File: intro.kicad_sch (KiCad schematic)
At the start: 122 parts, among them IC1 IS31FL3741A-QFLS4-TR, SW1 SW_Push, SW10 SW_Push, SW11 SW_Push, SW12 SW_Push, SW13 SW_Push, SW14 SW_Push, SW15 SW_Push, SW16 SW_Push, SW17 SW_Push, SW18 SW_Push, SW19 SW_Push, SW2 SW_Push, SW20 SW_Push, SW21 SW_Push, SW22 SW_Push, SW23 SW_Push, SW24 SW_Push, SW25 SW_Push, SW26 SW_Push, SW27 SW_Push, SW28 SW_Push, SW29 SW_Push, SW3 SW_Push, SW30 SW_Push, SW31 SW_Push, SW32 SW_Push, SW33 SW_Push, SW34 SW_Push, SW35 RotaryEncoder_Switch, SW4 SW_Push, SW5 SW_Push, SW6 SW_Push, SW7 SW_Push, SW8 SW_Push, SW9 SW_Push, U1 nice_nano

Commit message: Set up LED routing
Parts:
- removed S1, S2: Choc_stab, intro:Kailh-PG1350-2u-STAB, symbol marbastlib-mx:MX_stab
- added C10, C2, C8: 0.1μF, Capacitor_SMD:C_0805_2012Metric, symbol Device:C_Small
- added C3, C9: 1μF, Capacitor_SMD:C_0805_2012Metric, symbol Device:C_Small
- added IC2: IS31FL3741A-QFLS4-TR, QFN40P700X700X80-61N-D, symbol IS31FL3741A-QFLS4-TR:IS31FL3741A-QFLS4-TR
- added R10: 10kΩ, Resistor_SMD:R_0805_2012Metric, symbol Device:R_Small_US
- added R6, R9: 100kΩ, Resistor_SMD:R_0805_2012Metric, symbol Device:R_Small_US
- added R7, R8: 2kΩ, Resistor_SMD:R_0805_2012Metric, symbol Device:R_Small_US
- D1, D10, D11, D12, D13, D14, D15, D16, D17, D18, D19, D2, D20, D21, D22, D23, D24, D25, D26, D27, D28, D29, D3, D30, D31, D32, D33, D34, D35, D4, D5, D6, D7, D8, D9: footprint Diode_SMD:D_SOD-123 -> intro:D_SOD-123_Reversible
- LED1, LED10, LED11, LED12, LED13, LED14, LED15, LED16, LED17, LED18, LED19, LED2, LED20, LED21, LED22, LED23, LED24, LED25, LED26, LED27, LED28, LED29, LED3, LED30, LED31, LED32, LED33, LED34, LED35, LED36, LED37, LED4, LED5, LED6, LED7, LED8, LED9: footprint intro:FMB2020RGBAHG -> intro:FMB2020RGBAHG_Reversible
- SW1, SW14, SW15, SW29, SW33: footprint intro:SW_choc_1.5u -> intro:SW_choc_Reversible_1.5u
- SW10, SW11, SW12, SW13, SW16, SW17, SW18, SW19, SW2, SW20, SW21, SW22, SW23, SW24, SW25, SW26, SW27, SW28, SW3, SW30, SW31, SW4, SW5, SW6, SW7, SW8, SW9: footprint intro:SW_choc_1u -> intro:SW_choc_Reversible_1u
- SW32, SW34: footprint intro:SW_choc_1u -> intro:SW_choc_Reversible_2u_STAB
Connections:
- net CS1: now also IC2.26 (CS1)
- net CS10: now also IC2.38 (CS12)
- net CS11: now also IC2.37 (CS11)
- net CS12: now also IC2.35 (CS10)
- net CS13: now also IC2.34 (CS9)
- net CS14: now also IC2.33 (CS8)
- net CS15: now also IC2.44 (CS18)
- net CS16: now also IC2.43 (CS17)
- net CS17: now also IC2.42 (CS16)
- net CS18: now also IC2.41 (CS15)
- net CS19: now also IC2.45 (CS19)
- net CS2: now also IC2.27 (CS2)
- net CS20: now also IC2.46 (CS20)
- net CS3: now also IC2.28 (CS3)
- net CS4: now also IC2.29 (CS4)
- net CS5: now also IC2.30 (CS5)
- net CS6: now also IC2.32 (CS7)
- net CS7: now also IC2.31 (CS6)
- net CS8: now also IC2.40 (CS14)
- net CS9: now also IC2.39 (CS13)
- net GND: now also C10.2, C2.2, C3.2, C8.2, C9.2, IC2.12 (GND_1), IC2.36 (GND_2), IC2.55 (GND_3), IC2.61 (EP), IC2.8 (ADDR), R10.1, R9.2
- net INTB: now also IC2.7 (INTB), R6.2
- net RSW1: now also IC2.17 (SW2)
- net RSW2: now also IC2.18 (SW3)
- net RSW3: now also IC2.16 (SW1)
- net RSW4: now also IC2.20 (SW5)
- net RSW5: now also IC2.19 (SW4)
- net RSW6: now also IC2.21 (SW6)
- net SCL: now also IC2.10 (SCL), R7.2
- net SDA: now also IC2.9 (SDA), R8.2
- net SDB: now also C2.1, IC2.11 (SDB), R9.1
- net VCC: now also C10.1, C3.1, C8.1, C9.1, IC2.14 (AVCC), IC2.15 (PVCC_1), IC2.25 (PVCC_2), R6.1, R7.1, R8.1
- new net: IC2.13 (ISET), R10.2
- no-connect marks 25 -> 47
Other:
- moved on the sheet: C1, C4, C5, C6, C7, D1, D10, D11, D12, D13, D14, D15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

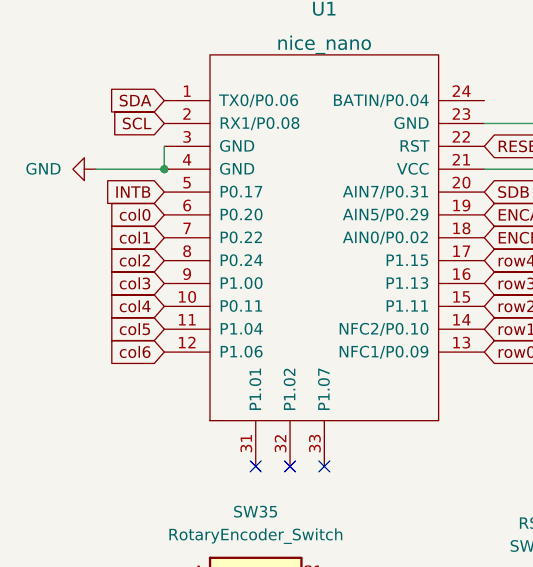
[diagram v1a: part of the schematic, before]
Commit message: Wiring switches & diodes
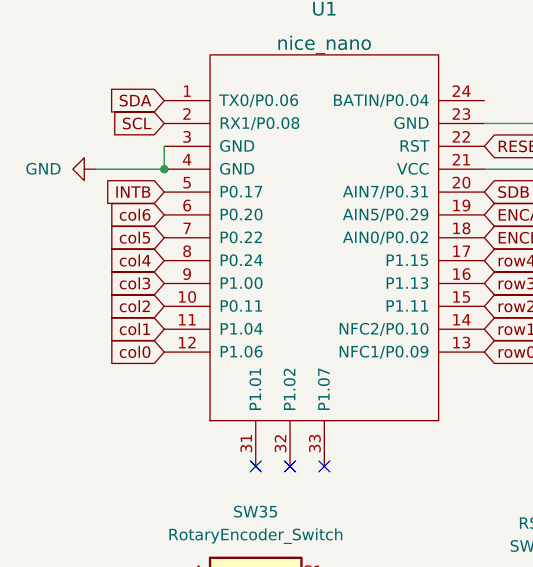
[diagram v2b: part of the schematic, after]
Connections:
- net SW35A: now also U1.6 (P0.20); no longer U1.12 (P1.06)
- net col0: now also U1.12 (P1.06); no longer U1.6 (P0.20)
- net col1: now also U1.11 (P1.04); no longer U1.7 (P0.22)
- net col2: now also U1.10 (P0.11); no longer U1.8 (P0.24)
- net col4: now also U1.8 (P0.24); no longer U1.10 (P0.11)
- net col5: now also U1.7 (P0.22); no longer U1.11 (P1.04)

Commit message: Progress
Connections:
- net CS1: now also IC1.43 (CS17); no longer IC1.26 (CS1)
- net CS10: now also IC1.51 (CS25); no longer IC1.38 (CS12)
- net CS11: now also IC1.50 (CS24); no longer IC1.37 (CS11)
- net CS12: now also IC1.49 (CS23); no longer IC1.35 (CS10)
- net CS13: now also IC1.48 (CS22); no longer IC1.34 (CS9)
- net CS14: now also IC1.40 (CS14); no longer IC1.33 (CS8)
- net CS15: now also IC1.54 (CS28); no longer IC1.44 (CS18)
- net CS16: now also IC1.56 (CS29); no longer IC1.43 (CS17)
- net CS17: now also IC1.57 (CS30); no longer IC1.42 (CS16)
- net CS18: now also IC1.58 (CS31); no longer IC1.41 (CS15)
- net CS19: now also IC1.59 (CS32), IC2.30 (CS5); no longer IC1.45 (CS19), IC2.45 (CS19)
- net CS2: now also IC1.44 (CS18); no longer IC1.27 (CS2)
- net CS20: now also IC1.60 (CS33), IC2.29 (CS4); no longer IC1.46 (CS20), IC2.46 (CS20)
- net CS3: now also IC1.45 (CS19); no longer IC1.28 (CS3)
- net CS4: now also IC1.47 (CS21); no longer IC1.29 (CS4), IC2.29 (CS4)
- net CS5: now also IC1.46 (CS20); no longer IC1.30 (CS5), IC2.30 (CS5)
- net CS6: now also IC1.42 (CS16); no longer IC1.32 (CS7)
- net CS7: now also IC1.41 (CS15); no longer IC1.31 (CS6)
- net CS8: now also IC1.53 (CS27); no longer IC1.40 (CS14)
- net CS9: now also IC1.52 (CS26); no longer IC1.39 (CS13)
- no-connect marks 47 -> 30
